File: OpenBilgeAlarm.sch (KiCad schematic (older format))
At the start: 13 parts

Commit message: More or less finished schematics, some stuff left to source
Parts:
- removed BT?: Battery_Cell, symbol Battery_Cell
- removed U?: 74HC595, symbol 74HC595
- removed U?: 7805, symbol 7805
- added C? (x2): CP, symbol CP
- added C? (x2): 1u, Capacitors_SMD:C_1210_HandSoldering, symbol C
- added C? (x5): C, Capacitors_SMD:C_0603_HandSoldering, symbol C
- added D? (x5): D_TVS, symbol D_TVS
- added D?: 48V, Diodes_SMD:Diode-SMB_Handsoldering, symbol D_TVS
- added D?: 24V, Diodes_SMD:Diode-SMA_Handsoldering, symbol D_Zener
- added D?: 16V, Diodes_SMD:D_SOD-323_HandSoldering, symbol D_Zener
- added F?: Polyfuse, symbol Polyfuse
- added J?: CONN_01X04, symbol CONN_01X04
- added J?: CONN_01X02, symbol CONN_01X02
- added Q? (x2): Q_NMOS_GSD, symbol Q_NMOS_GSD
- added Q?: Q_PMOS_GSD, symbol Q_PMOS_GSD
- added R?: 10R, Resistors_SMD:R_2512, symbol R
- added R?: 10k, symbol R
- added R? (x8): 330, Resistors_SMD:R_0603_HandSoldering, symbol R
- added R? (x3): 1k, Resistors_SMD:R_0603_HandSoldering, symbol R
- added R? (x6): 100k, Resistors_SMD:R_0603_HandSoldering, symbol R
- added RV?: POT, symbol POT
- added U?: 74HC595, symbol 74HC595
- Q?: value Q_PMOS_GSD -> Q; footprint (none) -> TO_SOT_Packages_SMD:TO-252-2Lead; symbol Q_PMOS_GSD -> Q_PMOS_GDS; Distributor (none) -> 2468040; Manufacturer (none) -> INFINEON; PartNo (none) -> IRFR5410TRPBF
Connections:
- net GND: now also DS?.1 (VSS), DS?.5 (R/W), SH?.GND1 (GND/1), SH?.GND2 (2/GND), SW?.1 (A), SW?.2 (C), SW?.4, U?.5 (GND), U?.GND, C?.2, C?.2, C?.2, C?.2, C?.2, C?.2, C?.2, C?.2, D?.2 (A), D?.2 (A2), D?.2 (A2), D?.2 (A2), D?.2 (A2), D?.2 (A2), D?.2 (A2), J?.1 (P1), J?.4 (P4), Q?.2 (S), Q?.2 (S), R?.1, R?.1, R?.1, R?.1, R?.1, R?.2, RV?.1, U?.13 (G), U?.8 (GND)
- net VCC: now also U?.16 (VCC)
- net RX: now reaches SH?.0 (RX)
- net RX: now also R?.1
- net TX: now reaches SH?.1 (TX)
- net TX: now also R?.1
- net LATCH: now reaches SH?.10 (10_(SS/*))
- net LATCH: now also R?.2, U?.12 (RCLK)
- net RGB_BLUE: now reaches SH?.11 (11_(MISO/*))
- net RGB_BLUE: now also R?.2
- net DATA: now reaches SH?.12 (12_(MOSI))
- net DATA: now also R?.2, U?.14 (SER)
- net SCK: now reaches SH?.13 (13_(SCK))
- net SCK: now also R?.2, U?.11 (SRCLK)
- net ENC_A: now reaches SH?.2
- net ENC_A: now also SW?.1 (A), C?.1, D?.1 (A1)
- net ENC_B: now reaches SH?.3 (3_(*))
- net ENC_B: now also SW?.3 (B), C?.1, D?.1 (A1)
- net ~READER_ENABLE: now reaches SH?.4
- net ~READER_ENABLE: now also R?.1
- net RGB_RED: now reaches SH?.5 (5_(*))
- net RGB_RED: now also R?.2
- net +5V: now reaches SH?.5V
- net +5V: now also D?.1 (A), D?.2 (A), LS?.1, U?.8 (VCC), U?.VO, C?.1, F?.1, Q?.2 (S), R?.2, R?.2, U?.10 (SRCLR)
- net RGB_GREEN: now reaches SH?.6 (6_(*))
- net RGB_GREEN: now also R?.2
- net BUTTON: now reaches SH?.7
- net BUTTON: now also SW?.2 (B), C?.1, D?.1 (A1)
- net LED: now reaches SH?.8
- net LED: now also R?.2
- net BUZZER: now reaches SH?.9 (9_(*))
- net BUZZER: now also R?.2, R?.2
- net ENC_BUTTON: now reaches SH?.A0
- net ENC_BUTTON: now also SW?.5, C?.1, D?.1 (A1)
- net LCD_POWER: now reaches SH?.A1
- net LCD_POWER: now also R?.1, R?.2
- net at DS?.11 (D4): now also U?.6 (QG)
- net at DS?.12 (D5): now also U?.5 (QF)
- net at DS?.13 (D6): now also U?.4 (QE)
- net at DS?.14 (D7): now also U?.3 (QD)
- net at DS?.15 (LED+): now also DS?.2 (VDD), Q?.3 (D), RV?.3
- net at DS?.16 (LED-): now also Q?.3 (D)
- net at DS?.3 (VO): now also RV?.2
- net at DS?.4 (RS): now also U?.1 (QB)
- net at DS?.6 (E): now also U?.2 (QC)
- net at LS?.2: now also Q?.3 (D), R?.1
- net at D?.1 (K): now also R?.1
- net at D?.2 (RK): now also R?.1
- net at D?.3 (GK): now also R?.1
- net at D?.4 (BK): now also R?.1
- net at U?.1 (RO): now also R?.2
- net at U?.2 (~RE~): now also U?.3 (DE), R?.2
- net at U?.4 (DI): now also R?.2
- net at U?.6 (A): now also J?.2 (P2)
- net at U?.7 (B): now also J?.3 (P3)
- net at U?.VI: now also Q?.3 (S), D?.1 (K)
- net at Q?.1 (G): now also D?.2 (A), R?.1
- net at Q?.2 (D): now also C?.1, D?.1 (K), R?.1
- new net: R?.2, R?.2, U?.7 (QH)
- new net: C?.1, C?.1, D?.1 (A1), F?.2, J?.1 (P1)
- new net: C?.1, D?.1 (A1), J?.2 (P2), R?.2
- new net: Q?.1 (G), R?.1 (x3)
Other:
- moved on the sheet: D?, DS?, LS?, Q?, SH?, SW?, U?

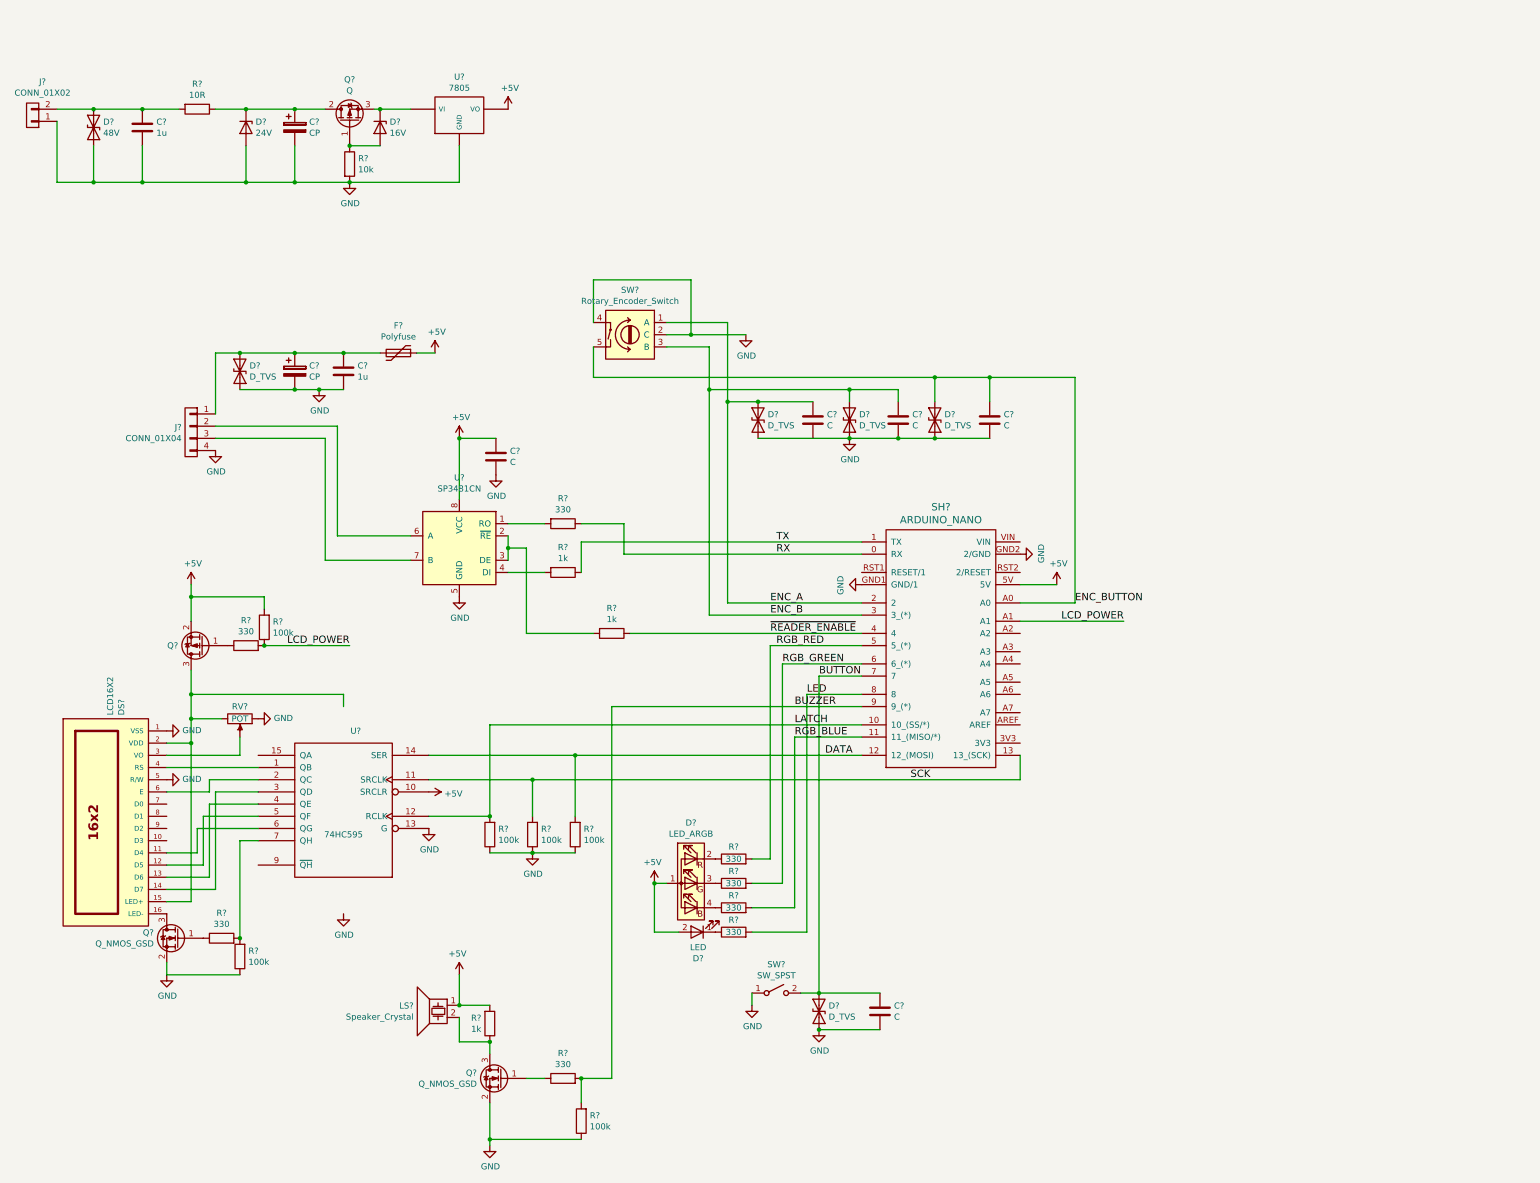
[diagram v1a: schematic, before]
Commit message: Throw everything on board, try to route, start solving the mechanical puzzle
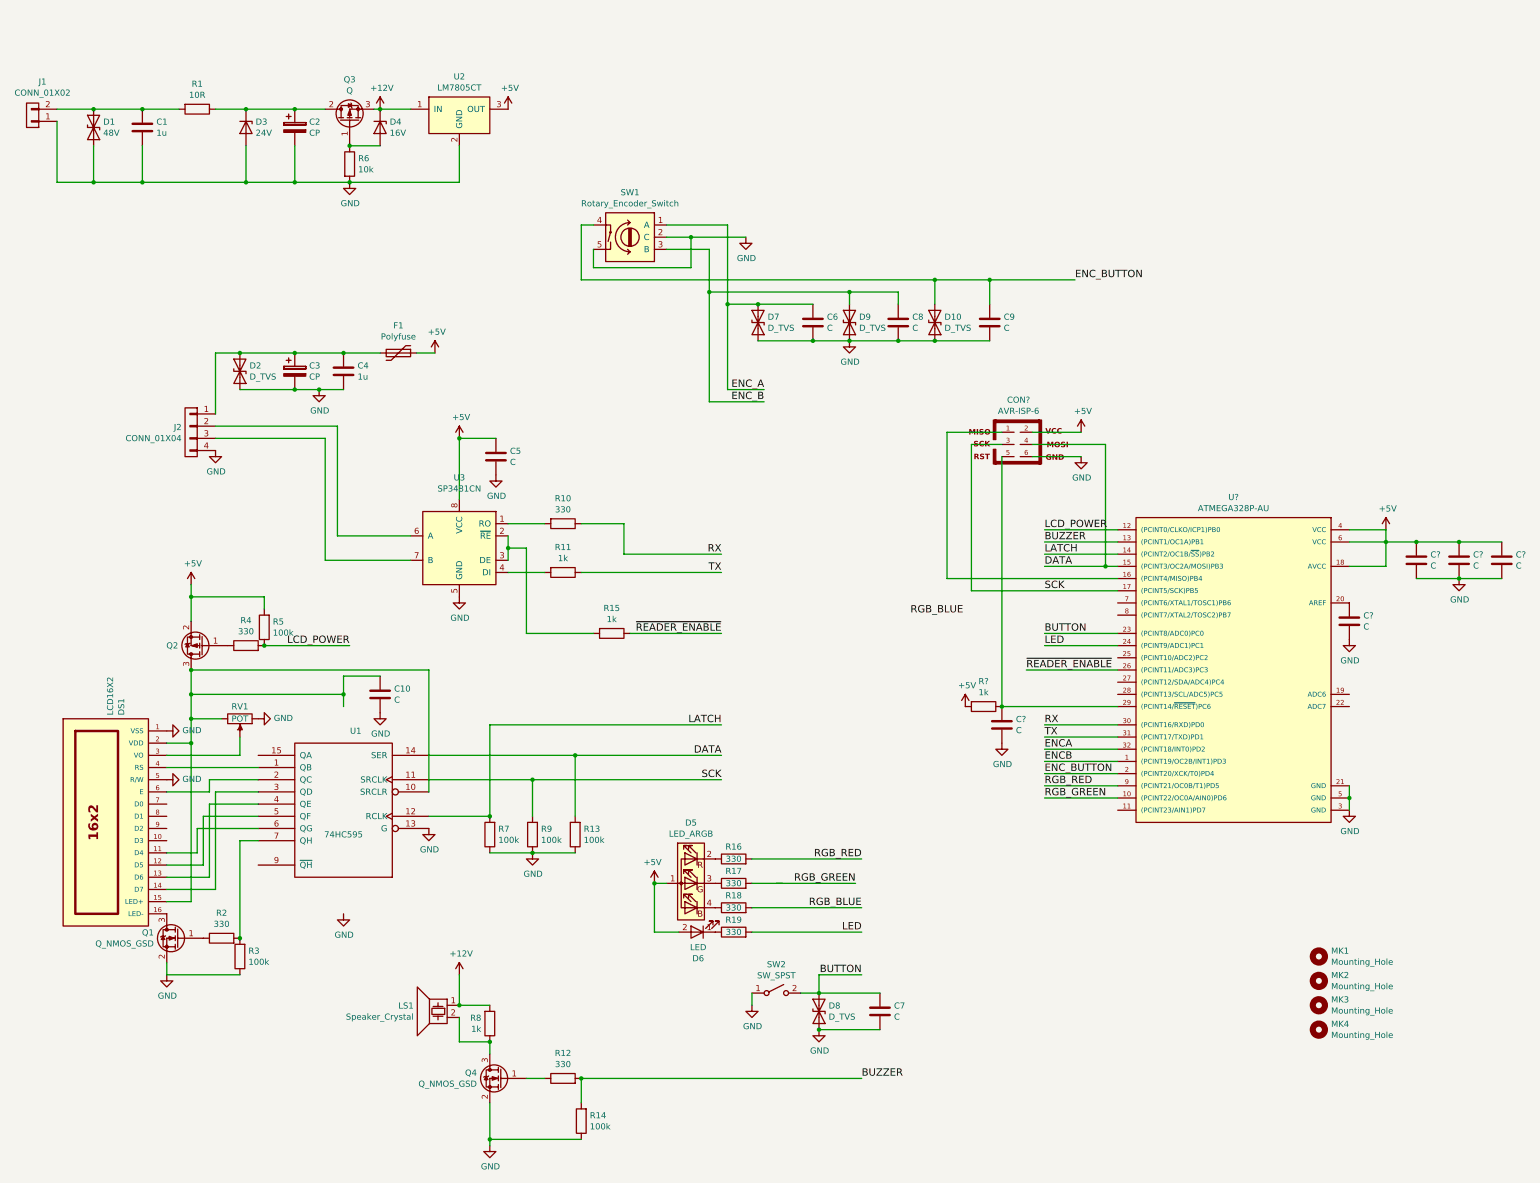
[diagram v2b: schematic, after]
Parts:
- removed D? (x4): D_TVS, symbol D_TVS
- removed SH?: ARDUINO_NANO, symbol ARDUINO_NANO
- removed U?: 7805, symbol 7805
- added C10, C? (x5): C, Capacitors_SMD:C_0603_HandSoldering, symbol C
- added CON?: AVR-ISP-6, Pin_Headers:Pin_Header_Straight_2x03_Pitch2.54mm, symbol AVR-ISP-6
- added D10, D2, D8, D9: D_TVS, Diodes_SMD:SOD-323, symbol D_TVS
- added MK1, MK2, MK3, MK4: Mounting_Hole, Mounting_Holes:MountingHole_3.2mm_M3, symbol Mounting_Hole
- added R?: 1k, Resistors_SMD:R_0603_HandSoldering, symbol R
- added U2: LM7805CT, TO_SOT_Packages_THT:TO-220_Vertical, symbol LM7805CT
- added U?: ATMEGA328P-AU, TQFP32, symbol ATMEGA328P-AU
- C2, C3: renamed from C?; footprint (none) -> Capacitors_ThroughHole:CP_Radial_D5.0mm_P2.50mm; Distributor (none) -> ?; Manufacturer (none) -> ?; PartNo (none) -> ?
- D5: renamed from D?; footprint (none) -> LEDs:LED_D5.0mm-4; Distributor (none) -> ?; Manufacturer (none) -> ?; PartNo (none) -> ?
- D6: renamed from D?; footprint (none) -> LEDs:LED_D5.0mm; Distributor (none) -> ?; Manufacturer (none) -> ?; PartNo (none) -> ?
- D7: renamed from D?; footprint (none) -> Diodes_SMD:SOD-323; Distributor (none) -> 2059012; Manufacturer (none) -> ?; PartNo (none) -> ?
- DS1: renamed from DS?; footprint WC1602A -> Displays:WC1602A; Distributor (none) -> ?; Manufacturer (none) -> ?; PartNo (none) -> ?
- F1: renamed from F?; footprint (none) -> Resistors_THT:R_Box_L8.4mm_W2.5mm_P5.08mm; Distributor (none) -> ?; Manufacturer (none) -> ?; PartNo (none) -> ?
- J1: renamed from J?; footprint (none) -> smalsiukas-footpints:TerminalBlock_5.08-2pol; Distributor (none) -> ?; Manufacturer (none) -> ?; PartNo (none) -> ?
- J2: renamed from J?; footprint (none) -> smalsiukas-footpints:TerminalBlock_5.08-5pol; Distributor (none) -> ?; Manufacturer (none) -> ?; PartNo (none) -> ?
- LS1: renamed from LS?; footprint (none) -> Buzzers_Beepers:Buzzer_12x9.5RM7.6; Distributor (none) -> 2135931; Manufacturer (none) -> ?; PartNo (none) -> ?
- Q1, Q2, Q4: renamed from Q?; footprint (none) -> TO_SOT_Packages_SMD:SOT-23_Handsoldering; Distributor (none) -> ?; Manufacturer (none) -> ?; PartNo (none) -> ?
- R6: renamed from R?; footprint (none) -> Resistors_SMD:R_0603_HandSoldering; Distributor (none) -> ?; Manufacturer (none) -> ?; PartNo (none) -> ?
- RV1: renamed from RV?; footprint (none) -> Potentiometers:Potentiometer_Trimmer_ACP_CA6v_Horizontal; Distributor (none) -> ?; Manufacturer (none) -> ?; PartNo (none) -> ?
- SW1: renamed from SW?; footprint (none) -> bilge-alarm-parts:Encoder_Bourns_PEC12R-4xxxF-Sxxxx; Distributor (none) -> 2663534; Manufacturer (none) -> ?; PartNo (none) -> ?
- SW2: renamed from SW?; footprint (none) -> Buttons_Switches_SMD:SW_SPST_EVPBF; Distributor (none) -> ?; Manufacturer (none) -> ?; PartNo (none) -> ?
- U1: renamed from U?; footprint (none) -> Housings_SOIC:SOIC-16_3.9x9.9mm_Pitch1.27mm; Distributor (none) -> ?; Manufacturer (none) -> ?; PartNo (none) -> ?
- gave numbers to parts that had none: 30
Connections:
- net +5V: now also C?.1, C?.1, C?.1, CON?.2, R?.2, U2.3 (OUT), U?.18 (AVCC), U?.4 (VCC), U?.6 (VCC); no longer LS1.1, R8.2, U1.10 (SRCLR)
- net BUTTON: now also D8.1 (A1), U?.23 ((PCINT8/ADC0)PC0)
- net BUZZER: now also U?.13 ((PCINT1/OC1A)PB1)
- net DATA: now also CON?.4, U?.15 ((PCINT3/OC2A/MOSI)PB3)
- net ENC_B: now also D9.1 (A1)
- net ENC_BUTTON: now also SW1.4, D10.1 (A1), U?.2 ((PCINT20/XCK/T0)PD4); no longer SW1.5
- net GND: now also C6.2, SW1.5, C10.2, C?.2, C?.2, C?.2, C?.2, C?.2, CON?.6, D10.2 (A2), D2.2 (A2), D8.2 (A2), D9.2 (A2), U2.2 (GND), U?.21 (GND), U?.3 (GND), U?.5 (GND); no longer SW1.4
- net LATCH: now also U?.14 ((PCINT2/OC1B/~SS~)PB2)
- net LCD_POWER: now also U?.12 ((PCINT0/CLKO/ICP1)PB0)
- net LED: now also U?.24 ((PCINT9/ADC1)PC1)
- net RGB_GREEN: now also U?.10 ((PCINT22/OC0A/AIN0)PD6)
- net RGB_RED: now also U?.9 ((PCINT21/OC0B/T1)PD5)
- net RX: now also U?.30 ((PCINT16/RXD)PD0)
- net SCK: now also CON?.3, U?.17 ((PCINT5/SCK)PB5)
- net TX: now also U?.31 ((PCINT17/TXD)PD1)
- net ~READER_ENABLE: now also U?.26 ((PCINT11/ADC3)PC3)
- net at DS1.15 (LED+), DS1.2 (VDD), Q2.3 (D)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: now also U1.10 (SRCLR), C10.1
- net +12V: now reaches D4.1 (K), Q3.3 (S)
- net +12V: now also LS1.1, R8.2, U2.1 (IN)
- net at C3.1, C4.1, F1.2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: now also D2.1 (A1)
- new net: CON?.1, U?.16 ((PCINT4/MISO)PB4)
- new net: C?.1, U?.20 (AREF)
- new net: C?.1, CON?.5, R?.1, U?.29 ((PCINT14/~RESET~)PC6)
- new net ENCA: U?.32 ((PCINT18/INT0)PD2)
- new net ENCB: U?.1 ((PCINT19/OC2B/INT1)PD3)
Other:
- moved on the sheet: C6, C8, C9, D7, SW1
